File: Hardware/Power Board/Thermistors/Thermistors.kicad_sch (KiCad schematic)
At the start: 5 parts, among them J1 Conn_01x05_MountingPin

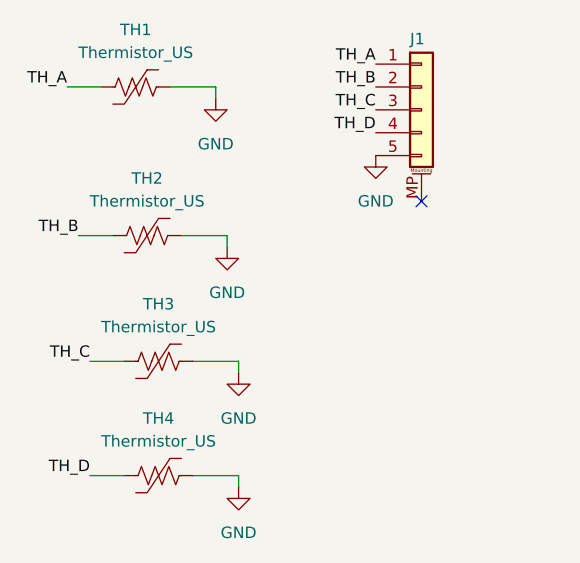
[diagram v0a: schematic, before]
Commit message: update to some firmware stuff and updates/fab stuff for the thermsitor board
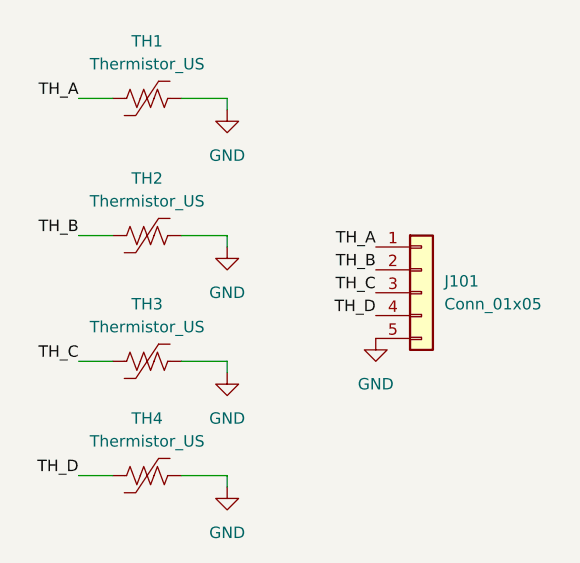
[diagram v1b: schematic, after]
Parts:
- removed J1: Conn_01x05_MountingPin, Connector_JST:JST_EH_B5B-EH-A_1x05_P2.50mm_Vertical, symbol Connector_Generic_MountingPin:Conn_01x05_MountingPin
- added J101: Conn_01x05, BAD_LIB:FPC_5pin, symbol Connector_Generic:Conn_01x05
- TH1, TH2, TH3, TH4: footprint Resistor_SMD:R_0603_1608Metric -> Resistor_SMD:R_0402_1005Metric
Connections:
- net GND: now also J101.5 (Pin_5)
- net TH_A: now also J101.1 (Pin_1)
- net TH_B: now also J101.2 (Pin_2)
- net TH_C: now also J101.3 (Pin_3)
- net TH_D: now also J101.4 (Pin_4)
- no-connect marks 1 -> 0
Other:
- moved on the sheet: TH1
